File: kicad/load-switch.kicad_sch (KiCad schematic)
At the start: 18 parts, among them Q7 IPA045N10N3G, T5 BC846B, U5 INA186

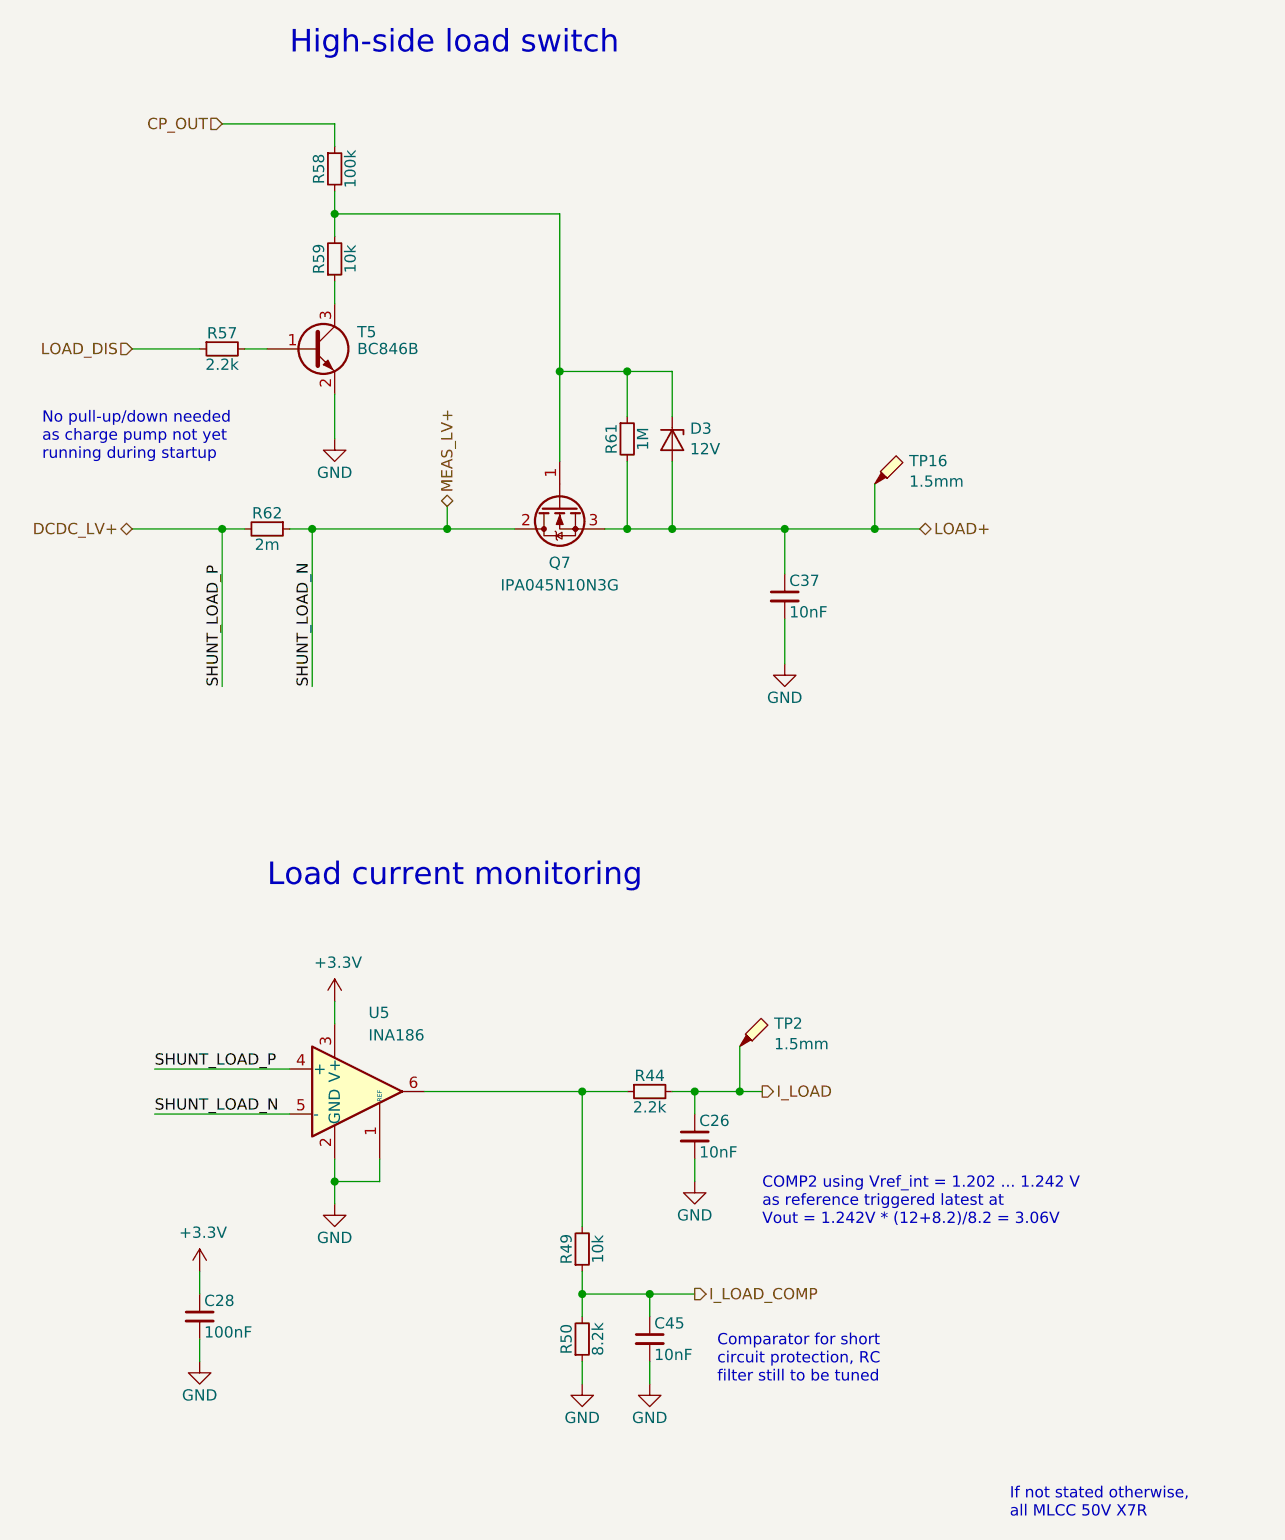
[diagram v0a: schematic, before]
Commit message: removed load terminal & circuit
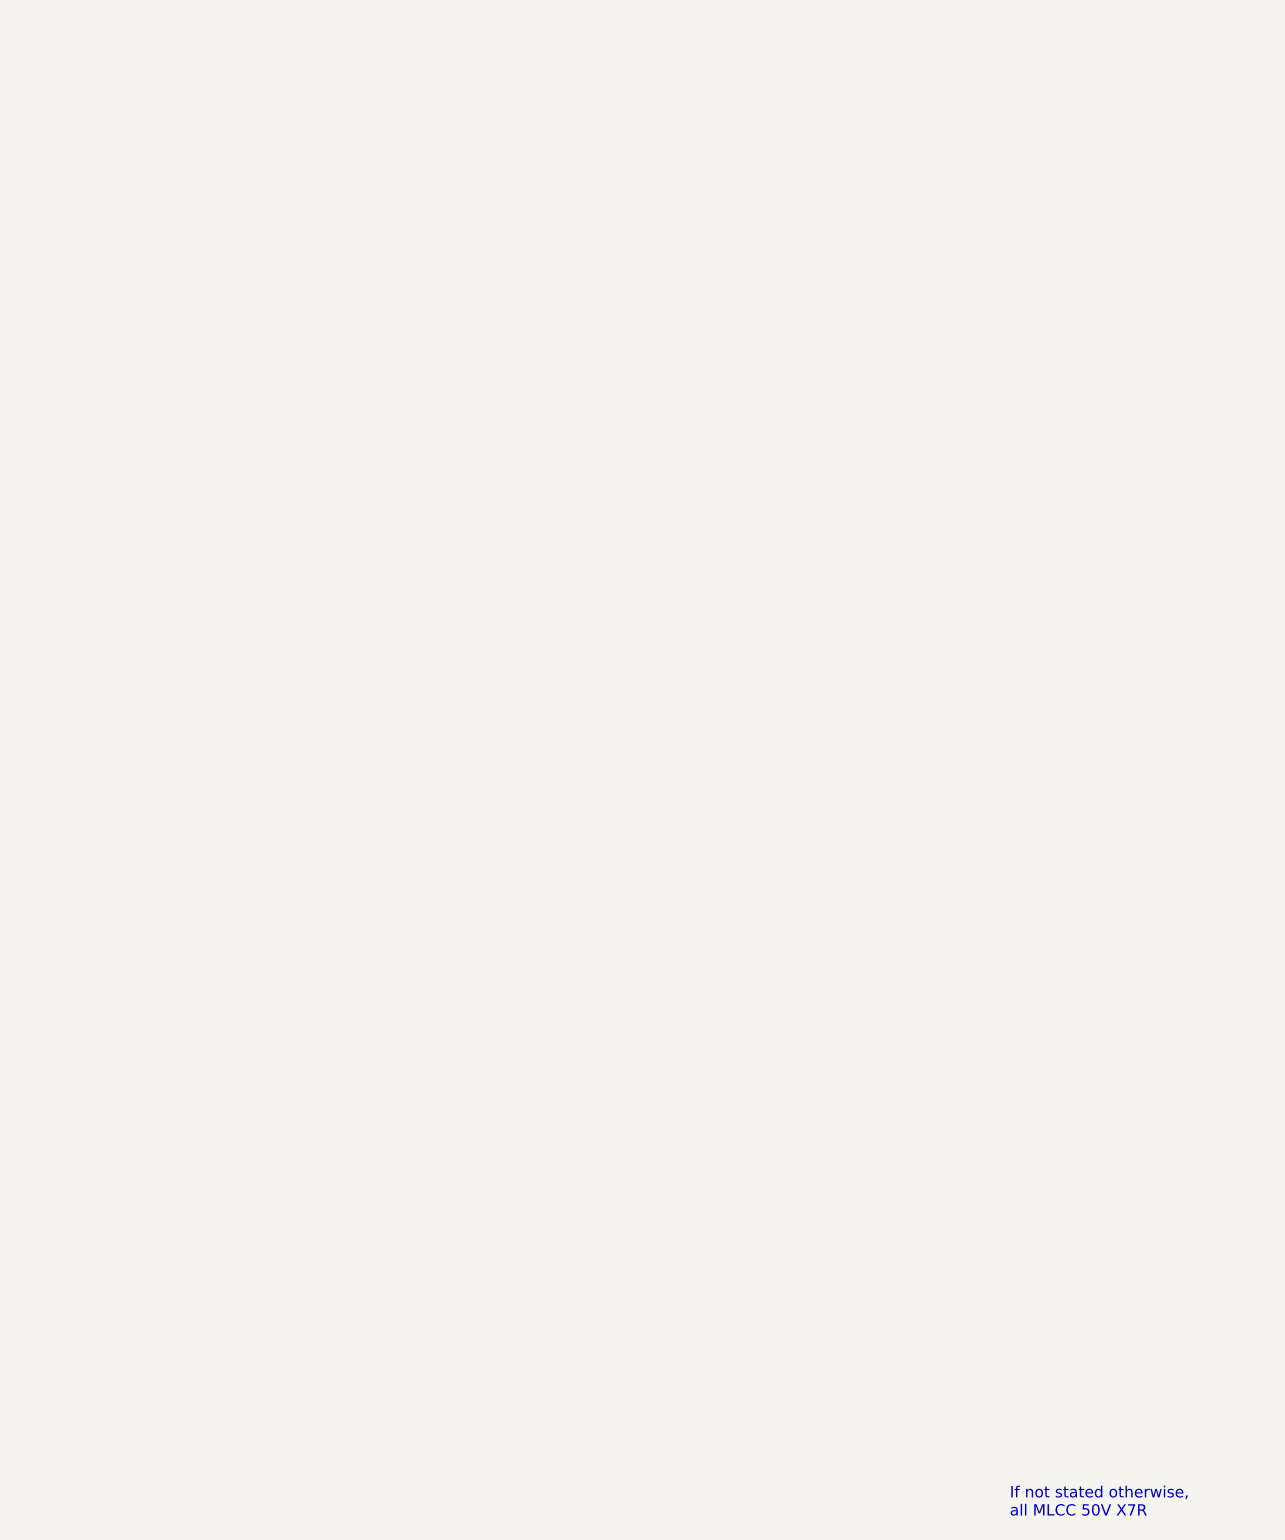
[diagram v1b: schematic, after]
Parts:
- removed C26, C37, C45: 10nF, LibreSolar:C_0603_1608, symbol Project:C
- removed C28: 100nF, LibreSolar:C_0603_1608, symbol Project:C
- removed D3: 12V, Diode_SMD:D_SOT-23_ANK, symbol Project:D_Zener
- removed Q7: IPA045N10N3G, LibreSolar:TO-220-3_Horizontal_BottomHeatsink, symbol Device:Q_NMOS_GDS
- removed R44, R57: 2.2k, LibreSolar:R_0603_1608, symbol Project:R
- removed R49, R59: 10k, LibreSolar:R_0603_1608, symbol Project:R
- removed R50: 8.2k, LibreSolar:C_0603_1608, symbol Project:R
- removed R58: 100k, LibreSolar:R_0603_1608, symbol Project:R
- removed R61: 1M, LibreSolar:R_0603_1608, symbol Project:R
- removed R62: 2m, LibreSolar:R_Bourns_CRE2512, symbol Project:R
- removed T5: BC846B, LibreSolar:SOT-23, symbol Transistor_BJT:BC846
- removed TP16, TP2: 1.5mm, TestPoint:TestPoint_Pad_D1.5mm, symbol Connector:TestPoint_Probe
- removed U5: INA186, Package_TO_SOT_SMD:SOT-363_SC-70-6, symbol mppt-2420-hc-rescue:INA186-LibreSolar
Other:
- note removed: "COMP2 using Vref_int = 1.202 ... 1.242 V as reference triggered latest at Vout = 1.242V * (12+8.2)/8.2 = 3.06V"
- note removed: "Comparator for short circuit protection, RC filter still to be tuned"
- note removed: "High-side load switch"
- note removed: "Load current monitoring"
- note removed: "No pull-up/down needed as charge pump not yet running during startup"
